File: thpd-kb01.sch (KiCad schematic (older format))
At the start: 39 parts, among them J1 USB_C_Receptacle_USB2.0, SW1 SW_Push, SW2 SW_SPDT, SW3 Rotary_Encoder_Switch, U1 XC6206PxxxMR, U2 USBLC6-2SC6, U3 NHD-C12832A1Z, U4 STM32F072C8Tx

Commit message: Add LCSC part numbers and prepared for output.
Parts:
- C1, C12, C13, C14, C15, C16, C17, C18, C19, C2, C7: LCSC Part # (none) -> C52923
- C10, C11, C4, C5, C6: LCSC Part # (none) -> C1525
- C20, C21, C8: LCSC Part # (none) -> C15195
- C3, C9: LCSC Part # (none) -> C23733
- F1: LCSC Part # (none) -> C135321
- J1: LCSC Part # (none) -> C165948
- R1, R2: LCSC Part # (none) -> C25905
- R3, R4: LCSC Part # (none) -> C25092
- R5, R6, R7, R8, R9: LCSC Part # (none) -> C25804
- SW1: LCSC Part # (none) -> C202388
- SW2: LCSC Part # (none) -> C128955
- U1: LCSC Part # (none) -> C5446
- U2: LCSC Part # (none) -> C2827654
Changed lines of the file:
@@
 F 2 "Fuse:Fuse_0603_1608Metric" H 5750 950 50  0001 L CNN
 F 3 "~" H 5700 1150 50  0001 C CNN
+F 4 "C135321" H 5700 1150 50  0001 C CNN "LCSC Part #"
 	1    5700 1150
 	0    1    1    0
@@
 F 2 "Connector_USB:USB_C_Receptacle_HRO_TYPE-C-31-M-12" H 1600 1750 50  0001 C CNN
 F 3 "https://www.usb.org/sites/default/files/documents/usb_type-c.zip" H 1600 1750 50  0001 C CNN
+F 4 "C165948" H 1450 1750 50  0001 C CNN "LCSC Part #"
 	1    1450 1750
 	1    0    0    -1
@@
 F 2 "Package_TO_SOT_SMD:SOT-23-6" H 4350 1450 50  0001 C CNN
 F 3 "https://www.st.com/resource/en/datasheet/usblc6-2.pdf" H 4550 2300 50  0001 C CNN
+F 4 "C2827654" H 4350 1950 50  0001 C CNN "LCSC Part #"
 	1    4350 1950
 	1    0    0    -1
@@
 F 2 "Resistor_SMD:R_0402_1005Metric" H 4900 1850 50  0001 C CNN
 F 3 "~" H 4900 1850 50  0001 C CNN
+F 4 "C25092" H 4900 1850 50  0001 C CNN "LCSC Part #"
 	1    4900 1850
 	0    1    1    0
@@
 F 2 "Package_TO_SOT_SMD:SOT-23" H 6450 1375 50  0001 C CIN
 F 3 "https://www.torexsemi.com/file/xc6206/XC6206.pdf" H 6450 1150 50  0001 C CNN
+F 4 "C5446" H 6450 1150 50  0001 C CNN "LCSC Part #"
 	1    6450 1150
 	1    0    0    -1
@@
 F 2 "Capacitor_SMD:C_0402_1005Metric" H 5950 1250 50  0001 C CNN
 F 3 "~" H 5950 1250 50  0001 C CNN
+F 4 "C52923" H 5950 1250 50  0001 C CNN "LCSC Part #"
 	1    5950 1250
 	1    0    0    -1
@@
 F 2 "Capacitor_SMD:C_0402_1005Metric" H 6850 1250 50  0001 C CNN
 F 3 "~" H 6850 1250 50  0001 C CNN
+F 4 "C52923" H 6850 1250 50  0001 C CNN "LCSC Part #"
 	1    6850 1250
 	1    0    0    -1
@@
 F 2 "Button_Switch_SMD:SW_Push_SPST_NO_Alps_SKRK" H 1300 3800 50  0001 C CNN
 F 3 "~" H 1300 3800 50  0001 C CNN
+F 4 "C202388" H 1300 3600 50  0001 C CNN "LCSC Part #"
 	1    1300 3600
 	1    0    0    -1
@@
 F 2 "Capacitor_SMD:C_0402_1005Metric" H 1300 3850 50  0001 C CNN
 F 3 "~" H 1300 3850 50  0001 C CNN
+F 4 "C1525" H 1300 3850 50  0001 C CNN "LCSC Part #"
 	1    1300 3850
 	0    1    1    0
@@
 F 2 "Capacitor_SMD:C_0402_1005Metric" H 8000 1350 50  0001 C CNN
 F 3 "~" H 8000 1350 50  0001 C CNN
+F 4 "C23733" H 8000 1350 50  0001 C CNN "LCSC Part #"
 	1    8000 1350
 	1    0    0    -1
@@
 F 2 "Capacitor_SMD:C_0402_1005Metric" H 8350 1350 50  0001 C CNN
 F 3 "~" H 8350 1350 50  0001 C CNN
+F 4 "C1525" H 8350 1350 50  0001 C CNN "LCSC Part #"
 	1    8350 1350
 	1    0    0    -1
@@
 F 2 "Capacitor_SMD:C_0402_1005Metric" H 8700 1350 50  0001 C CNN
 F 3 "~" H 8700 1350 50  0001 C CNN
+F 4 "C1525" H 8700 1350 50  0001 C CNN "LCSC Part #"
 	1    8700 1350
 	1    0    0    -1
@@
 F 2 "Capacitor_SMD:C_0402_1005Metric" H 9050 1350 50  0001 C CNN
 F 3 "~" H 9050 1350 50  0001 C CNN
+F 4 "C1525" H 9050 1350 50  0001 C CNN "LCSC Part #"
 	1    9050 1350
 	1    0    0    -1
@@
 F 2 "Capacitor_SMD:C_0402_1005Metric" H 9400 1350 50  0001 C CNN
 F 3 "~" H 9400 1350 50  0001 C CNN
+F 4 "C52923" H 9400 1350 50  0001 C CNN "LCSC Part #"
 	1    9400 1350
 	1    0    0    -1
@@
 F 2 "Capacitor_SMD:C_0402_1005Metric" H 9750 1350 50  0001 C CNN
 F 3 "~" H 9750 1350 50  0001 C CNN
+F 4 "C15195" H 9750 1350 50  0001 C CNN "LCSC Part #"
 	1    9750 1350
 	1    0    0    -1
@@
 F 2 "Capacitor_SMD:C_0402_1005Metric" H 10100 1350 50  0001 C CNN
 F 3 "~" H 10100 1350 50  0001 C CNN
+F 4 "C23733" H 10100 1350 50  0001 C CNN "LCSC Part #"
 	1    10100 1350
 	1    0    0    -1
@@
 F 2 "Capacitor_SMD:C_0402_1005Metric" H 10450 1350 50  0001 C CNN
 F 3 "~" H 10450 1350 50  0001 C CNN
+F 4 "C1525" H 10450 1350 50  0001 C CNN "LCSC Part #"
 	1    10450 1350
 	1    0    0    -1
@@
 F 2 "Resistor_SMD:R_0402_1005Metric" H 2350 1450 50  0001 C CNN
 F 3 "~" H 2350 1450 50  0001 C CNN
+F 4 "C25905" H 2350 1450 50  0001 C CNN "LCSC Part #"
 	1    2350 1450
 	0    1    1    0
@@
 F 2 "Resistor_SMD:R_0402_1005Metric" H 2350 1350 50  0001 C CNN
 F 3 "~" H 2350 1350 50  0001 C CNN
+F 4 "C25905" H 2350 1350 50  0001 C CNN "LCSC Part #"
 	1    2350 1350
 	0    -1   -1   0
@@
 F 2 "Capacitor_SMD:C_0402_1005Metric" H 9050 5100 50  0001 C CNN
 F 3 "~" H 9050 5100 50  0001 C CNN
+F 4 "C52923" H 9050 5100 50  0001 C CNN "LCSC Part #"
 	1    9050 5100
 	1    0    0    -1
@@
 F 2 "Capacitor_SMD:C_0402_1005Metric" H 9400 5100 50  0001 C CNN
 F 3 "~" H 9400 5100 50  0001 C CNN
+F 4 "C52923" H 9400 5100 50  0001 C CNN "LCSC Part #"
 	1    9400 5100
 	1    0    0    -1
@@
 F 2 "Capacitor_SMD:C_0402_1005Metric" H 9750 5100 50  0001 C CNN
 F 3 "~" H 9750 5100 50  0001 C CNN
+F 4 "C52923" H 9750 5100 50  0001 C CNN "LCSC Part #"
 	1    9750 5100
 	1    0    0    -1
@@
 F 2 "Capacitor_SMD:C_0402_1005Metric" H 10100 5100 50  0001 C CNN
 F 3 "~" H 10100 5100 50  0001 C CNN
+F 4 "C52923" H 10100 5100 50  0001 C CNN "LCSC Part #"
 	1    10100 5100
 	1    0    0    -1
@@
 F 2 "Capacitor_SMD:C_0402_1005Metric" H 10450 5100 50  0001 C CNN
 F 3 "~" H 10450 5100 50  0001 C CNN
+F 4 "C52923" H 10450 5100 50  0001 C CNN "LCSC Part #"
 	1    10450 5100
 	1    0    0    -1
@@
 F 2 "Capacitor_SMD:C_0402_1005Metric" H 8500 5600 50  0001 C CNN
 F 3 "~" H 8500 5600 50  0001 C CNN
+F 4 "C52923" H 8500 5600 50  0001 C CNN "LCSC Part #"
 	1    8500 5600
 	1    0    0    -1
@@
 F 2 "Capacitor_SMD:C_0402_1005Metric" H 8950 4050 50  0001 C CNN
 F 3 "~" H 8950 4050 50  0001 C CNN
+F 4 "C52923" H 8950 4050 50  0001 C CNN "LCSC Part #"
 	1    8950 4050
 	1    0    0    -1
@@
 F 2 "Capacitor_SMD:C_0402_1005Metric" H 8950 4350 50  0001 C CNN
 F 3 "~" H 8950 4350 50  0001 C CNN
+F 4 "C52923" H 8950 4350 50  0001 C CNN "LCSC Part #"
 	1    8950 4350
 	1    0    0    -1
@@
 F 2 "Resistor_SMD:R_0402_1005Metric" H 3800 1850 50  0001 C CNN
 F 3 "~" H 3800 1850 50  0001 C CNN
+F 4 "C25092" H 3800 1850 50  0001 C CNN "LCSC Part #"
 	1    3800 1850
 	0    1    1    0
@@
 F 2 "Resistor_SMD:R_0603_1608Metric" H 1750 5800 50  0001 C CNN
 F 3 "~" H 1750 5800 50  0001 C CNN
+F 4 "C25804" H 1750 5800 50  0001 C CNN "LCSC Part #"
 	1    1750 5800
 	-1   0    0    1
@@
 F 2 "Resistor_SMD:R_0603_1608Metric" H 1450 5800 50  0001 C CNN
 F 3 "~" H 1450 5800 50  0001 C CNN
+F 4 "C25804" H 1450 5800 50  0001 C CNN "LCSC Part #"
 	1    1450 5800
 	-1   0    0    1
@@
 F 2 "Resistor_SMD:R_0603_1608Metric" H 1900 6200 50  0001 C CNN
 F 3 "~" H 1900 6200 50  0001 C CNN
+F 4 "C25804" H 1900 6200 50  0001 C CNN "LCSC Part #"
 	1    1900 6200
 	0    1    1    0
@@
 F 2 "Resistor_SMD:R_0603_1608Metric" H 1300 6200 50  0001 C CNN
 F 3 "~" H 1300 6200 50  0001 C CNN
+F 4 "C25804" H 1300 6200 50  0001 C CNN "LCSC Part #"
 	1    1300 6200
 	0    1    1    0
@@
 F 2 "Capacitor_SMD:C_0402_1005Metric" H 1150 6350 50  0001 C CNN
 F 3 "~" H 1150 6350 50  0001 C CNN
+F 4 "C15195" H 1150 6350 50  0001 C CNN "LCSC Part #"
 	1    1150 6350
 	-1   0    0    1
@@
 F 2 "Capacitor_SMD:C_0402_1005Metric" H 2100 6350 50  0001 C CNN
 F 3 "~" H 2100 6350 50  0001 C CNN
+F 4 "C15195" H 2100 6350 50  0001 C CNN "LCSC Part #"
 	1    2100 6350
 	1    0    0    -1
@@
 F 2 "thpd-kb01-custom:SW_SPDT_K3-1296S-E1" H 1350 4800 50  0001 C CNN
 F 3 "~" H 1350 4800 50  0001 C CNN
+F 4 "C128955" H 1350 4800 50  0001 C CNN "LCSC Part #"
 	1    1350 4800
 	-1   0    0    1
@@
 F 2 "Resistor_SMD:R_0603_1608Metric" H 1750 4800 50  0001 C CNN
 F 3 "~" H 1750 4800 50  0001 C CNN
+F 4 "C25804" H 1750 4800 50  0001 C CNN "LCSC Part #"
 	1    1750 4800
 	0    1    1    0

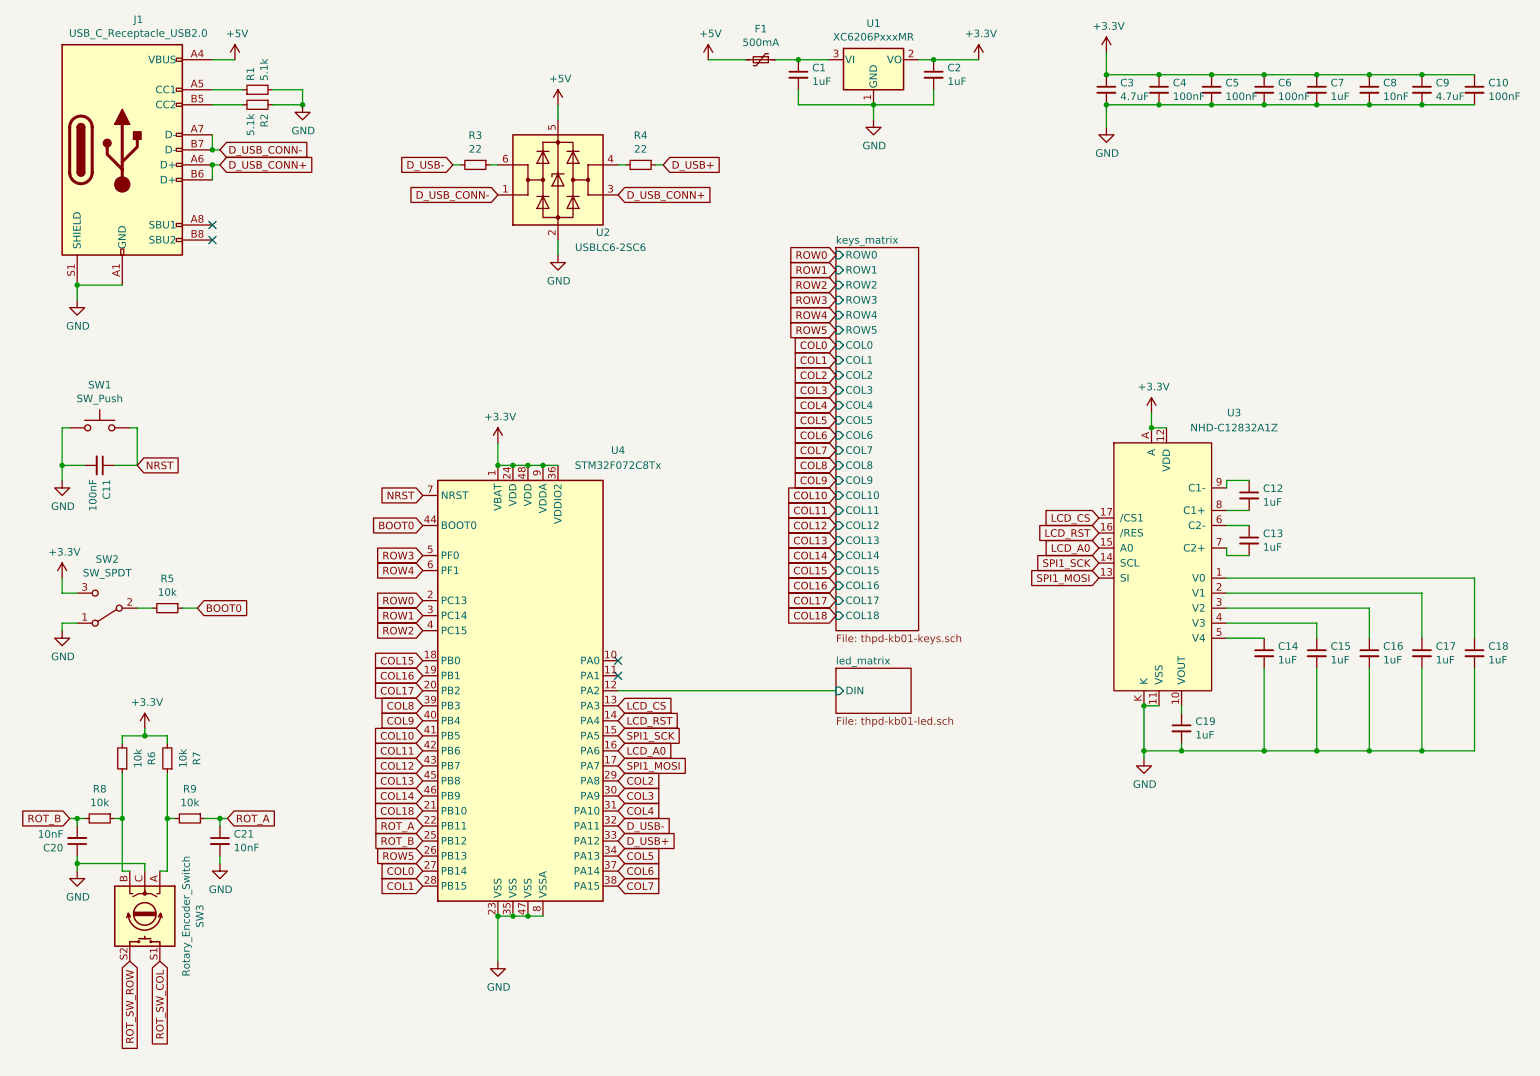
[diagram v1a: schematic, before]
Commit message: Remove LEDs and redo routing from scratch.
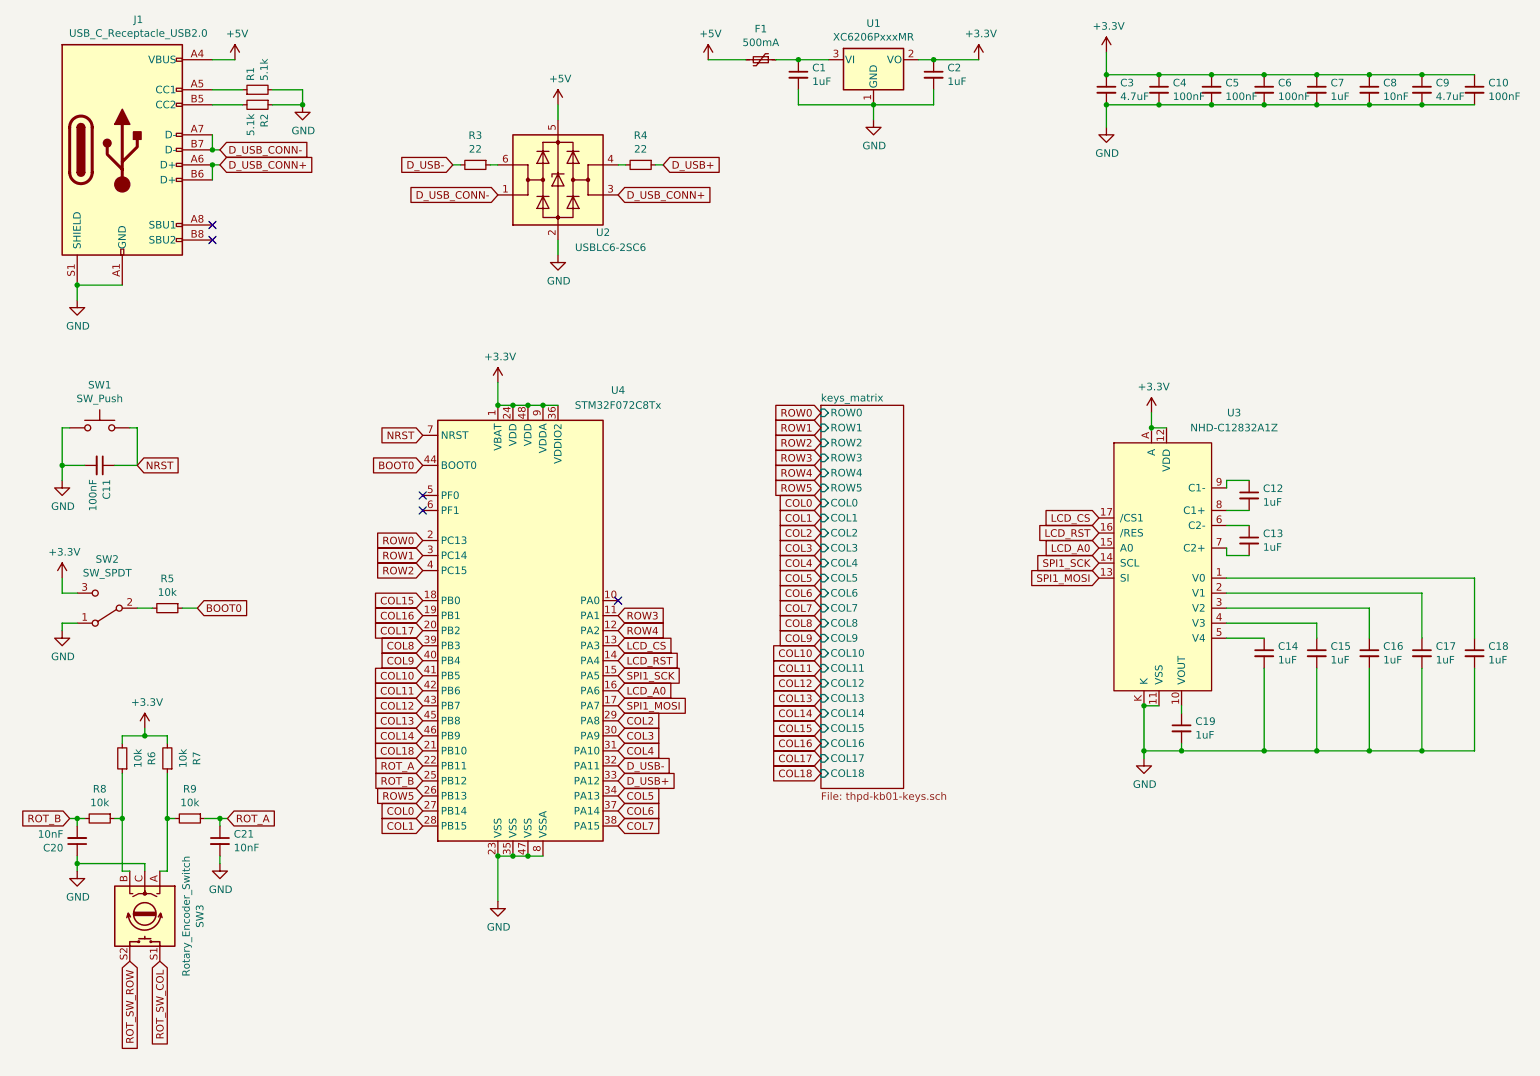
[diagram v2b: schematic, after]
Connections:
- net led_matrix/DIN is gone; now on net ROW4: U4.12 (PA2)
- net ROW3: now also U4.11 (PA1); no longer U4.5 (PF0)
- net ROW4: no longer U4.6 (PF1)
- no-connect marks 4 -> 5
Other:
- moved on the sheet: U4
